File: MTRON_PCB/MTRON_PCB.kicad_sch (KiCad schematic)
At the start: 44 parts

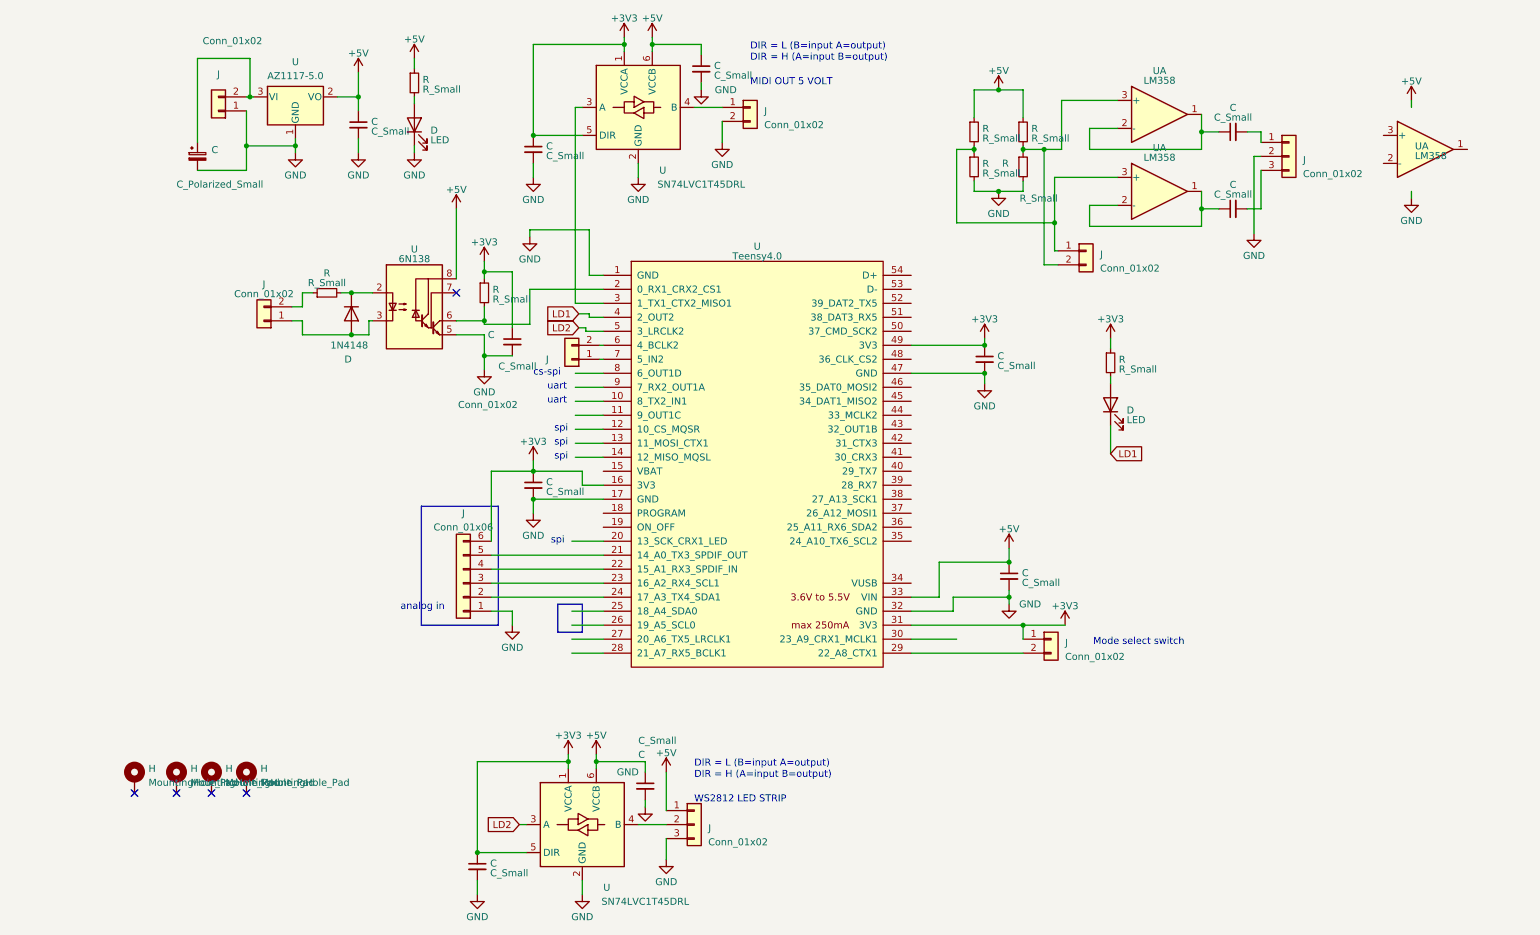
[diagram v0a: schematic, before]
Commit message: update design files, new version has less parts
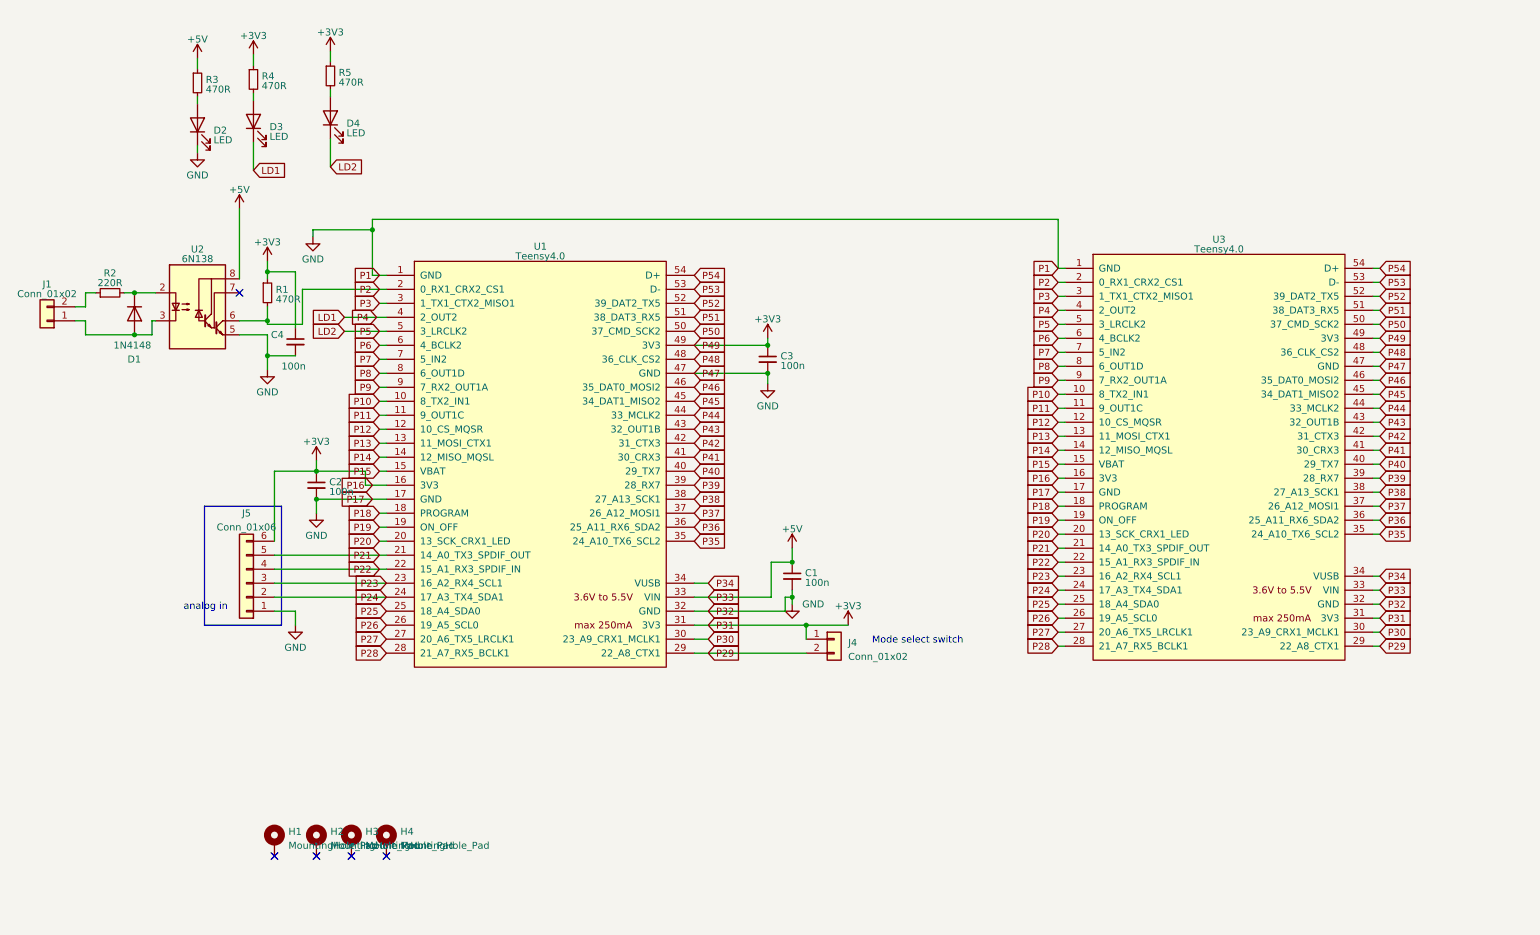
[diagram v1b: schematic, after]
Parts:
- removed C (x7): C_Small, symbol Device:C_Small
- removed C: C_Polarized_Small, symbol Device:C_Polarized_Small
- removed J (x4): Conn_01x02, symbol Connector_Generic:Conn_01x02
- removed J (x2): Conn_01x02, symbol Connector_Generic:Conn_01x03
- removed R (x4): R_Small, symbol Device:R_Small
- removed U (x2): SN74LVC1T45DRL, Package_TO_SOT_SMD:SOT-563, symbol Logic_LevelTranslator:SN74LVC1T45DRL
- removed U (x3): LM358, symbol Amplifier_Operational:LM358
- removed U: AZ1117-5.0, symbol Regulator_Linear:AZ1117-5.0
- added D4: LED, LED_THT:LED_D3.0mm_Horizontal_O6.35mm_Z6.0mm, symbol Device:LED
- added R5: 470R, Resistor_SMD:R_0805_2012Metric_Pad1.20x1.40mm_HandSolder, symbol Device:R_Small
- added U3: Teensy4.0, TeensyLibrary:Teensy40, symbol teensy:Teensy4.0
- C1, C2, C3, C4: renamed from C; value C_Small -> 100n; footprint (none) -> Capacitor_SMD:C_0805_2012Metric_Pad1.18x1.45mm_HandSolder
- D1: renamed from D; footprint Diode_THT:D_DO-35_SOD27_P7.62mm_Horizontal -> Diode_SMD:D_SOD-123
- D2, D3: renamed from D; footprint (none) -> LED_SMD:LED_0805_2012Metric
- H1, H2, H3, H4: renamed from H; footprint (none) -> MountingHole:MountingHole_3mm_Pad_Via
- J1, J4: renamed from J; footprint (none) -> Connector_PinHeader_2.54mm:PinHeader_1x02_P2.54mm_Vertical
- J5: renamed from J; footprint (none) -> Connector_PinHeader_2.54mm:PinHeader_1x06_P2.54mm_Vertical
- R1, R3, R4: renamed from R; value R_Small -> 470R; footprint (none) -> Resistor_SMD:R_0805_2012Metric_Pad1.20x1.40mm_HandSolder
- R2: renamed from R; value R_Small -> 220R; footprint (none) -> Resistor_SMD:R_0805_2012Metric_Pad1.20x1.40mm_HandSolder
- U1: renamed from U; footprint (none) -> TeensyLibrary:Teensy40
- U2: renamed from U; footprint (none) -> Package_DIP:DIP-8_W7.62mm_LongPads
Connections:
- net +3V3: now also R5.1, U3.16 (3V3), U3.31 (3V3), U3.49 (3V3)
- net +5V: now also U3.33 (VIN)
- net GND: now also U3.1 (GND), U3.17 (GND), U3.32 (GND), U3.47 (GND)
- net LD1: now also U3.4 (2_OUT2)
- net LD2: now also D4.1 (K), U3.5 (3_LRCLK2)
- net P2: now reaches R1.2, U1.2 (0_RX1_CRX2_CS1), U2.6 (VO2)
- net P2: now also U3.2 (0_RX1_CRX2_CS1)
- net P3: now reaches U1.3 (1_TX1_CTX2_MISO1)
- net P3: now also U3.3 (1_TX1_CTX2_MISO1)
- net P24: now reaches J5.2 (Pin_2), U1.24 (17_A3_TX4_SDA1)
- net P24: now also U3.24 (17_A3_TX4_SDA1)
- net P23: now reaches J5.3 (Pin_3), U1.23 (16_A2_RX4_SCL1)
- net P23: now also U3.23 (16_A2_RX4_SCL1)
- net P22: now reaches J5.4 (Pin_4), U1.22 (15_A1_RX3_SPDIF_IN)
- net P22: now also U3.22 (15_A1_RX3_SPDIF_IN)
- net P21: now reaches J5.5 (Pin_5), U1.21 (14_A0_TX3_SPDIF_OUT)
- net P21: now also U3.21 (14_A0_TX3_SPDIF_OUT)
- net P29: now reaches J4.2 (Pin_2), U1.29 (22_A8_CTX1)
- net P29: now also U3.29 (22_A8_CTX1)
- net P7: now reaches U1.7 (5_IN2)
- net P7: now also U3.7 (5_IN2)
- net P6: now reaches U1.6 (4_BCLK2)
- net P6: now also U3.6 (4_BCLK2)
- net P10: now reaches U1.10 (8_TX2_IN1)
- net P10: now also U3.10 (8_TX2_IN1)
- net P11: now reaches U1.11 (9_OUT1C)
- net P11: now also U3.11 (9_OUT1C)
- net P12: now reaches U1.12 (10_CS_MQSR)
- net P12: now also U3.12 (10_CS_MQSR)
- net P13: now reaches U1.13 (11_MOSI_CTX1)
- net P13: now also U3.13 (11_MOSI_CTX1)
- net P14: now reaches U1.14 (12_MISO_MQSL)
- net P14: now also U3.14 (12_MISO_MQSL)
- net P15: now reaches U1.15 (VBAT)
- net P15: now also U3.15 (VBAT)
- net P18: now reaches U1.18 (PROGRAM)
- net P18: now also U3.18 (PROGRAM)
- net P19: now reaches U1.19 (ON_OFF)
- net P19: now also U3.19 (ON_OFF)
- net P20: now reaches U1.20 (13_SCK_CRX1_LED)
- net P20: now also U3.20 (13_SCK_CRX1_LED)
- net P25: now reaches U1.25 (18_A4_SDA0)
- net P25: now also U3.25 (18_A4_SDA0)
- net P26: now reaches U1.26 (19_A5_SCL0)
- net P26: now also U3.26 (19_A5_SCL0)
- net P27: now reaches U1.27 (20_A6_TX5_LRCLK1)
- net P27: now also U3.27 (20_A6_TX5_LRCLK1)
- net P28: now reaches U1.28 (21_A7_RX5_BCLK1)
- net P28: now also U3.28 (21_A7_RX5_BCLK1)
- net P30: now reaches U1.30 (23_A9_CRX1_MCLK1)
- net P30: now also U3.30 (23_A9_CRX1_MCLK1)
- net P34: now reaches U1.34 (VUSB)
- net P34: now also U3.34 (VUSB)
- net P35: now reaches U1.35 (24_A10_TX6_SCL2)
- net P35: now also U3.35 (24_A10_TX6_SCL2)
- net P36: now reaches U1.36 (25_A11_RX6_SDA2)
- net P36: now also U3.36 (25_A11_RX6_SDA2)
- net P37: now reaches U1.37 (26_A12_MOSI1)
- net P37: now also U3.37 (26_A12_MOSI1)
- net P38: now reaches U1.38 (27_A13_SCK1)
- net P38: now also U3.38 (27_A13_SCK1)
- net P39: now reaches U1.39 (28_RX7)
- net P39: now also U3.39 (28_RX7)
- net P40: now reaches U1.40 (29_TX7)
- net P40: now also U3.40 (29_TX7)
- net P41: now reaches U1.41 (30_CRX3)
- net P41: now also U3.41 (30_CRX3)
- net P42: now reaches U1.42 (31_CTX3)
- net P42: now also U3.42 (31_CTX3)
- net P43: now reaches U1.43 (32_OUT1B)
- net P43: now also U3.43 (32_OUT1B)
- net P44: now reaches U1.44 (33_MCLK2)
- net P44: now also U3.44 (33_MCLK2)
- net P45: now reaches U1.45 (34_DAT1_MISO2)
- net P45: now also U3.45 (34_DAT1_MISO2)
- net P46: now reaches U1.46 (35_DAT0_MOSI2)
- net P46: now also U3.46 (35_DAT0_MOSI2)
- net P48: now reaches U1.48 (36_CLK_CS2)
- net P48: now also U3.48 (36_CLK_CS2)
- net P50: now reaches U1.50 (37_CMD_SCK2)
- net P50: now also U3.50 (37_CMD_SCK2)
- net P51: now reaches U1.51 (38_DAT3_RX5)
- net P51: now also U3.51 (38_DAT3_RX5)
- net P52: now reaches U1.52 (39_DAT2_TX5)
- net P52: now also U3.52 (39_DAT2_TX5)
- net P53: now reaches U1.53 (D-)
- net P53: now also U3.53 (D-)
- net P54: now reaches U1.54 (D+)
- net P54: now also U3.54 (D+)
- net P8: now reaches U1.8 (6_OUT1D)
- net P8: now also U3.8 (6_OUT1D)
- net P9: now reaches U1.9 (7_RX2_OUT1A)
- net P9: now also U3.9 (7_RX2_OUT1A)
- new net: D4.2 (A), R5.2
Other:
- note removed: "DIR = L (B=input A=output) DIR = H (A=input B=output)"
- note removed: "MIDI OUT 5 VOLT"
- note removed: "WS2812 LED STRIP"
- note removed: "cs-spi"
- note removed: "spi"
- note removed: "uart"
- moved on the sheet: C1, C2, C3, C4, D1, D2, D3, H1, H2, H3, H4, J1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

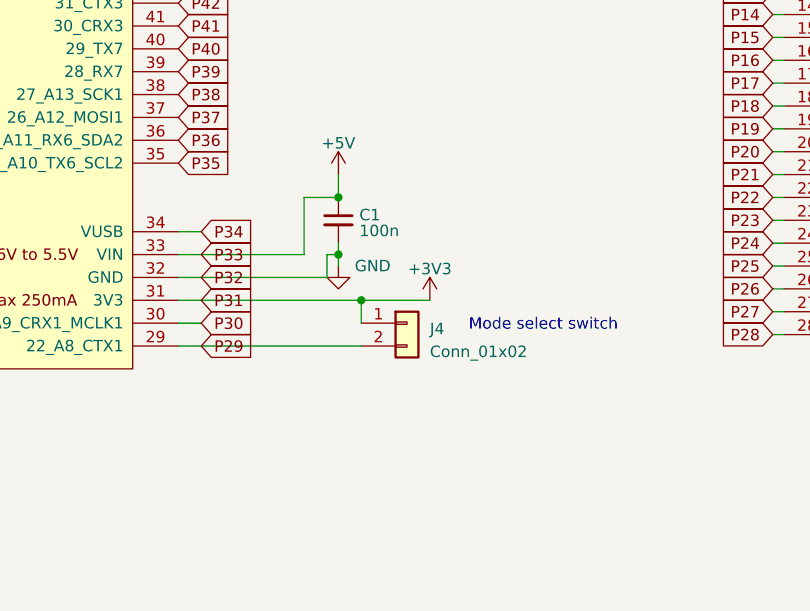
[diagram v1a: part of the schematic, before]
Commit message: nieuwe versie met alles THT en pull up voor switch. connector voor power. flip van linker device orientatie
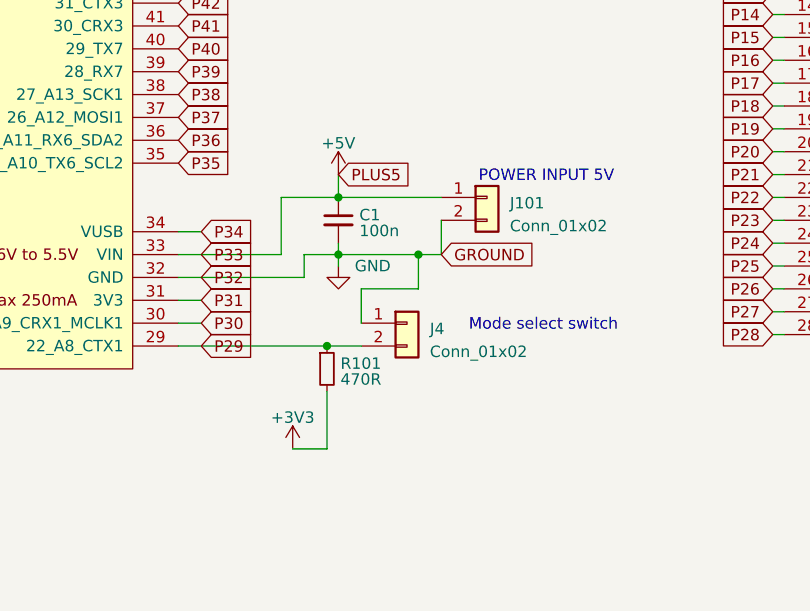
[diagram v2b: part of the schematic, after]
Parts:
- added J101: Conn_01x02, Connector_PinHeader_2.54mm:PinHeader_1x02_P2.54mm_Vertical, symbol Connector_Generic:Conn_01x02
- added R101: 470R, Resistor_THT:R_Axial_DIN0207_L6.3mm_D2.5mm_P7.62mm_Horizontal, symbol Device:R_Small
- C1, C2, C3, C4: footprint Capacitor_SMD:C_0805_2012Metric_Pad1.18x1.45mm_HandSolder -> Capacitor_THT:C_Disc_D4.7mm_W2.5mm_P5.00mm
- D1: footprint Diode_SMD:D_SOD-123 -> Diode_THT:D_DO-35_SOD27_P7.62mm_Horizontal
- D2, D3: footprint LED_SMD:LED_0805_2012Metric -> LED_THT:LED_D3.0mm
- D4: footprint LED_THT:LED_D3.0mm_Horizontal_O6.35mm_Z6.0mm -> LED_THT:LED_D3.0mm
- R1, R2, R3, R4, R5: footprint Resistor_SMD:R_0805_2012Metric_Pad1.20x1.40mm_HandSolder -> Resistor_THT:R_Axial_DIN0207_L6.3mm_D2.5mm_P7.62mm_Horizontal
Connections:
- net +3V3: now also R101.2; no longer J4.1 (Pin_1), U1.31 (3V3), U3.31 (3V3)
- net +5V: now also J101.1 (Pin_1)
- net GND: now also J4.1 (Pin_1), J101.2 (Pin_2)
- net P29: now also R101.1
- new net P31: U1.31 (3V3), U3.31 (3V3)
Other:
- note added: "POWER INPUT 5V"

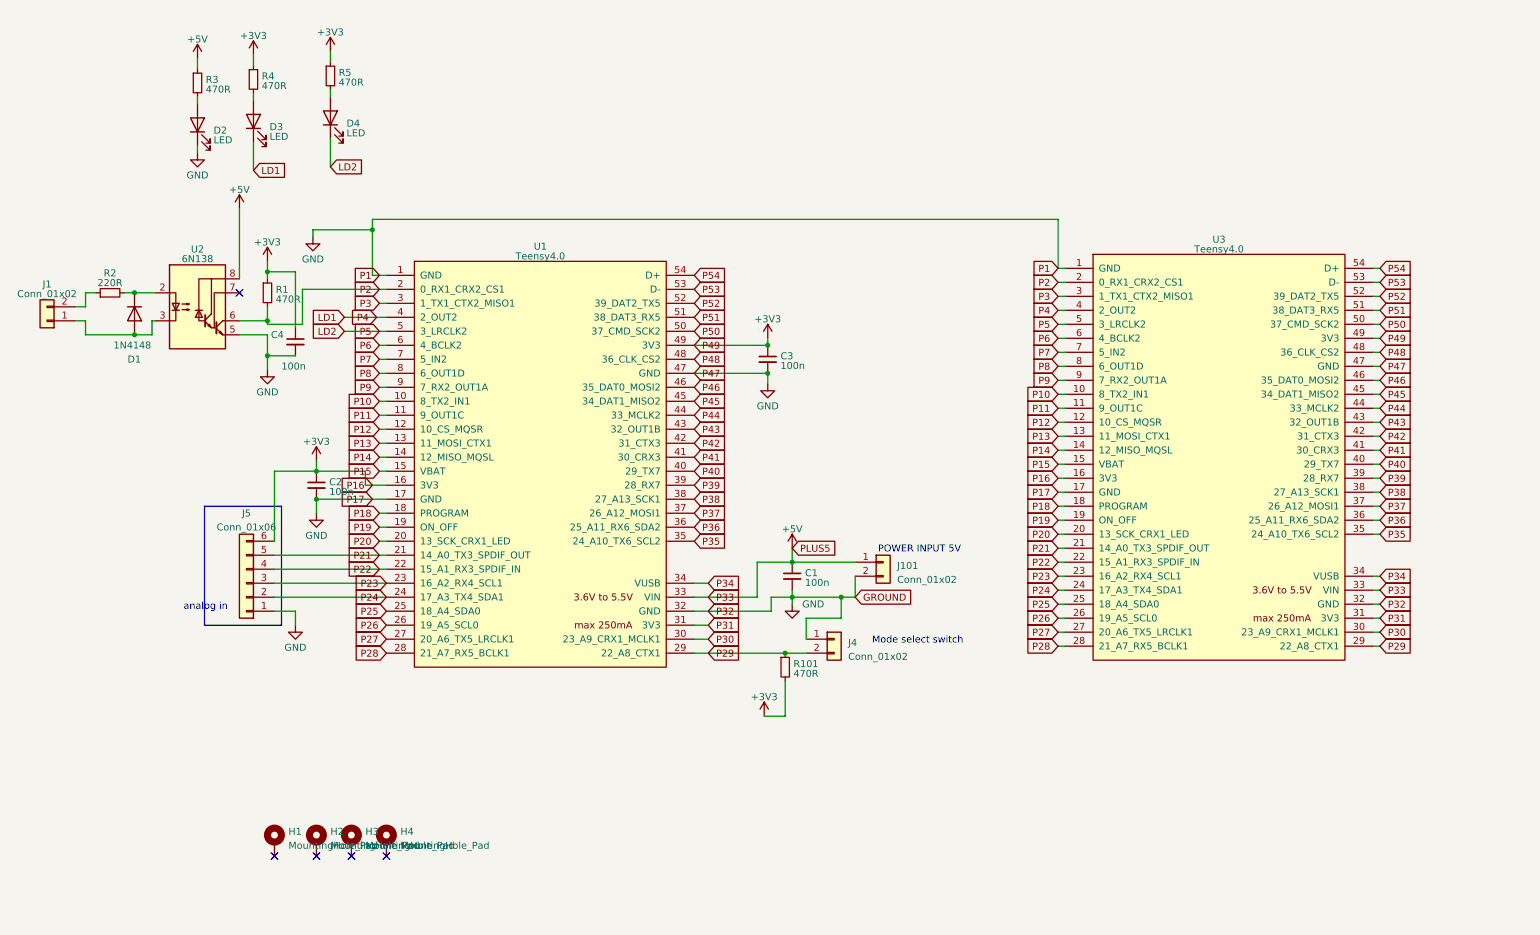
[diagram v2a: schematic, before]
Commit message: new version, includes fix for 3v3, audio transformer, logo, based on new findings.
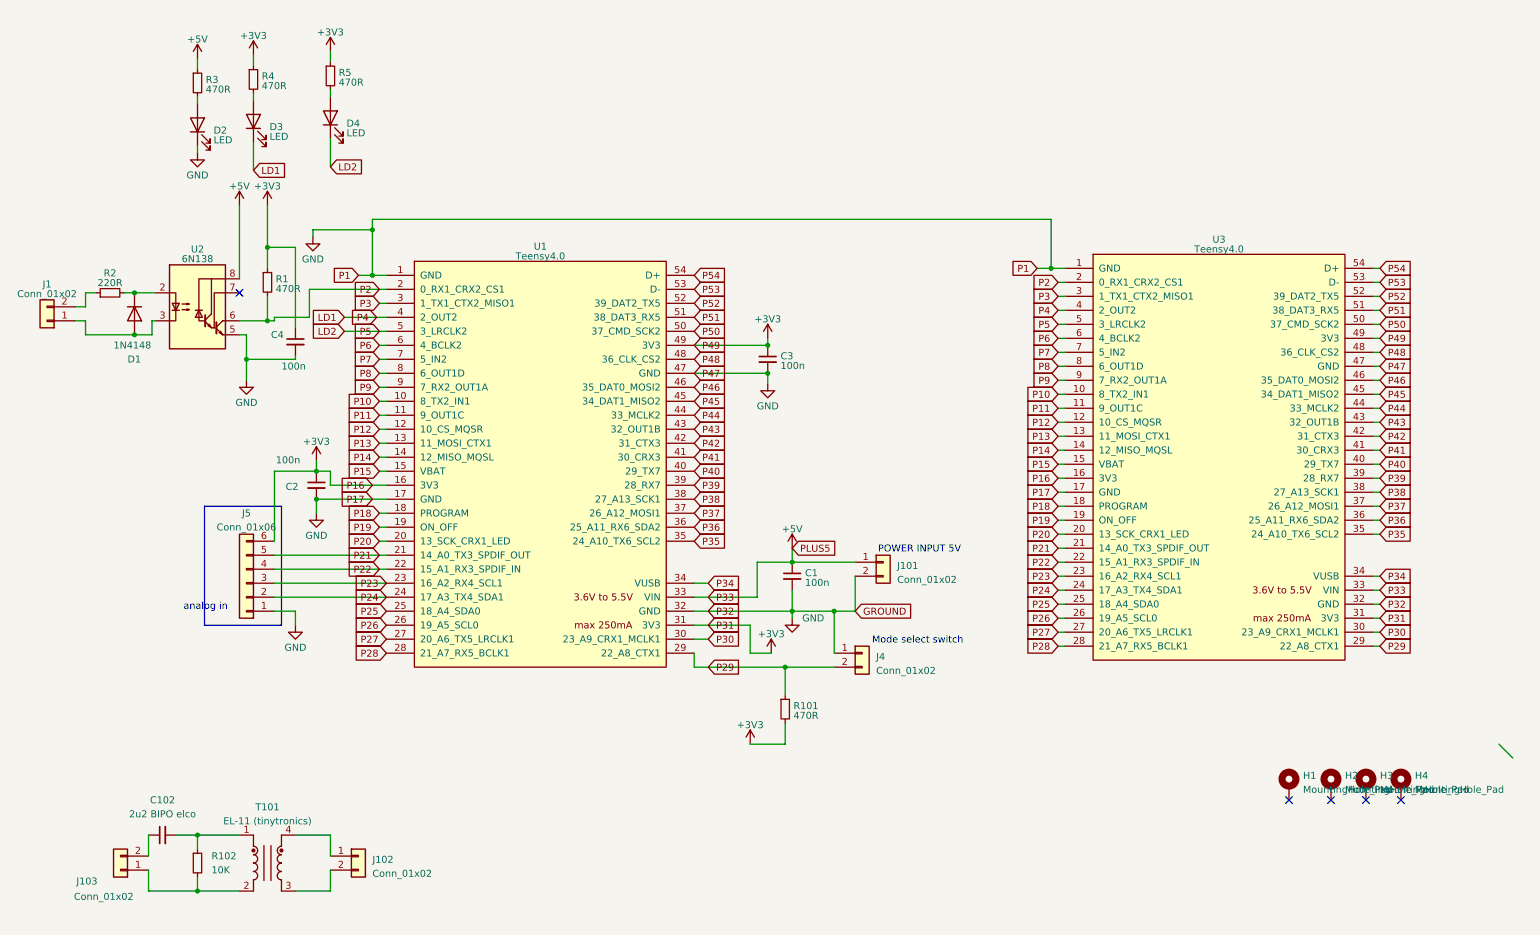
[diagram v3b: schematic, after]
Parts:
- added C102: 2u2 BIPO elco, Capacitor_THT:C_Radial_D5.0mm_H11.0mm_P2.00mm, symbol Device:C_Small
- added J102, J103: Conn_01x02, Connector_PinHeader_2.54mm:PinHeader_1x02_P2.54mm_Vertical, symbol Connector_Generic:Conn_01x02
- added R102: 10K, Resistor_THT:R_Axial_DIN0207_L6.3mm_D2.5mm_P7.62mm_Horizontal, symbol Device:R_Small
- added T101: EL-11 (tinytronics), AudioTransformer_Edwin:Transformer_EL-11-tinytronics, symbol Transformer:ED8_4
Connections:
- net P31 is gone; now on net +3V3: U1.31 (3V3), U3.31 (3V3)
- new net: C102.1, J103.2 (Pin_2)
- new net: C102.2, R102.1, T101.1
- new net: J103.1 (Pin_1), R102.2, T101.2
- new net: J102.2 (Pin_2), T101.3
- new net: J102.1 (Pin_1), T101.4
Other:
- moved on the sheet: H1, H2, H3, H4, J4, R1, R101
